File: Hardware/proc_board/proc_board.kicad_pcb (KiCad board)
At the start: 2 copper layers, 80.8 x 60.1 mm, 15 parts, among them J1 Conn_01x40, U1 GAL16V8, U2 W65C02SxP, U3 HM62256BLP, U4 28C256

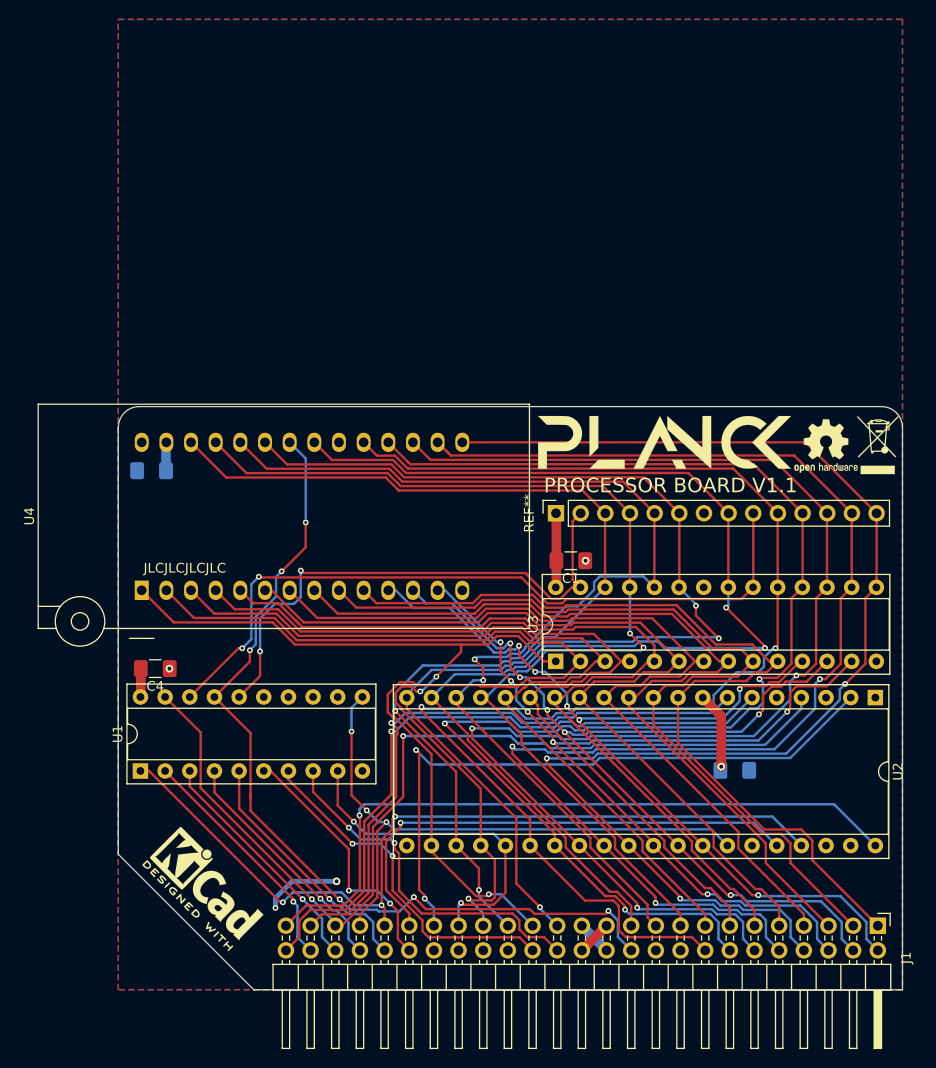
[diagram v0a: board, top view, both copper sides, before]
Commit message: Through hole components for processor board
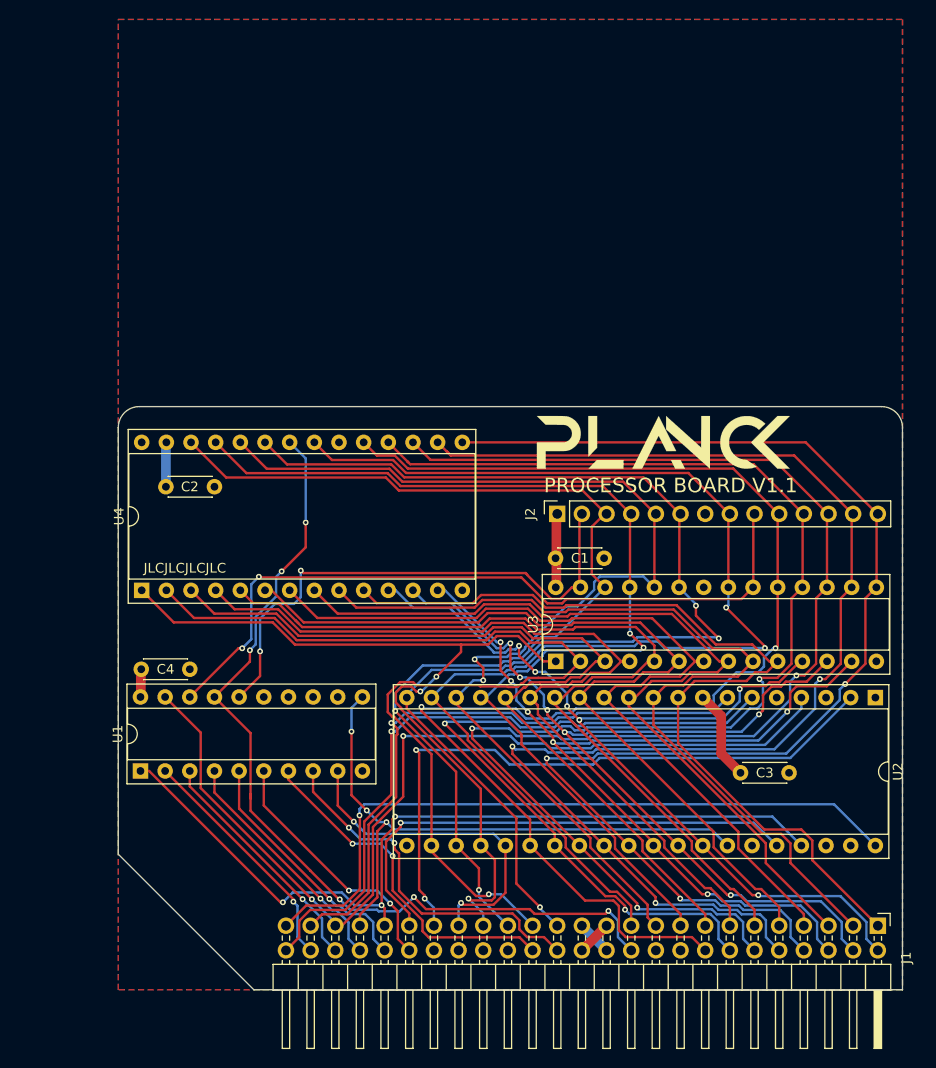
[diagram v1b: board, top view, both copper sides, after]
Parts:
- removed C5: C_Small, Capacitor_SMD:C_1206_3216Metric_Pad1.42x1.75mm_HandSolder
- removed the G*** at (65.9, -55.9)
- removed the G*** at (56.3, -56.4)
- removed REF**: PinSocket_1x14_P2.54mm_Vertical, Connector_PinSocket_2.54mm:PinSocket_1x14_P2.54mm_Vertical
- removed REF**: OSHW-Logo2_7.3x6mm_SilkScreen, Symbol:OSHW-Logo2_7.3x6mm_SilkScreen
- removed REF**: WEEE-Logo_4.2x6mm_SilkScreen, Symbol:WEEE-Logo_4.2x6mm_SilkScreen
- removed REF**: KiCad-Logo2_5mm_SilkScreen, Symbol:KiCad-Logo2_5mm_SilkScreen
- added C2: C_Small, Capacitor_THT:C_Disc_D4.3mm_W1.9mm_P5.00mm, F.Cu at (9.91, -51.8)
- added G***: LOGO, Logo:logo, B.Cu at (65.8, -56.4)
- added G***: LOGO, Logo:logo, F.Cu at (56.1, -56.4)
- added J2: Conn_01x14, Connector_PinSocket_2.54mm:PinSocket_1x14_P2.54mm_Vertical, F.Cu at (45.2, -49.0)
- C1, C4: footprint Capacitor_SMD:C_1206_3216Metric_Pad1.42x1.75mm_HandSolder -> Capacitor_THT:C_Disc_D4.3mm_W1.9mm_P5.00mm
- C3: footprint Capacitor_SMD:C_1206_3216Metric_Pad1.42x1.75mm_HandSolder -> Capacitor_THT:C_Disc_D4.3mm_W1.9mm_P5.00mm; moved to F.Cu
- U4: footprint Socket:DIP_Socket-28_W11.9_W12.7_W15.24_W17.78_W18.5_3M_228-1277-00-0602J -> Package_DIP:DIP-28_W15.24mm_Socket
- moved C3 5.59 mm to (69.1, -22.4)
- moved C4 3.56 mm to (7.37, -33.0)
- moved C1 3.44 mm to (50.0, -44.5)
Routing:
- net +5V: track 33.1 -> 28.2 mm, vias 3 -> 0
- net A13: track 108.3 -> 109.5 mm
- net ~RAMW~: track 55.6 -> 55.1 mm
- net GND: vias 2 -> 0

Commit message: Update gerbers
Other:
- rule pad_to_mask_clearance: 0.05 -> 0
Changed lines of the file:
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@@
     (pad_size 1.7 1.7)
     (pad_drill 1)
-    (pad_to_mask_clearance 0.05)
+    (pad_to_mask_clearance 0)
     (aux_axis_origin 0 0)
     (visible_elements FFFFFF7F)

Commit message: small updates to this deprecated board
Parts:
- C1, C2, C3, C4: value C_Small -> 10n
